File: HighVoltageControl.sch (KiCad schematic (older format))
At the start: 6 parts, among them Q1 DMG2302U, U1 NCS1S1205SC, U7 AZ1117-3.3

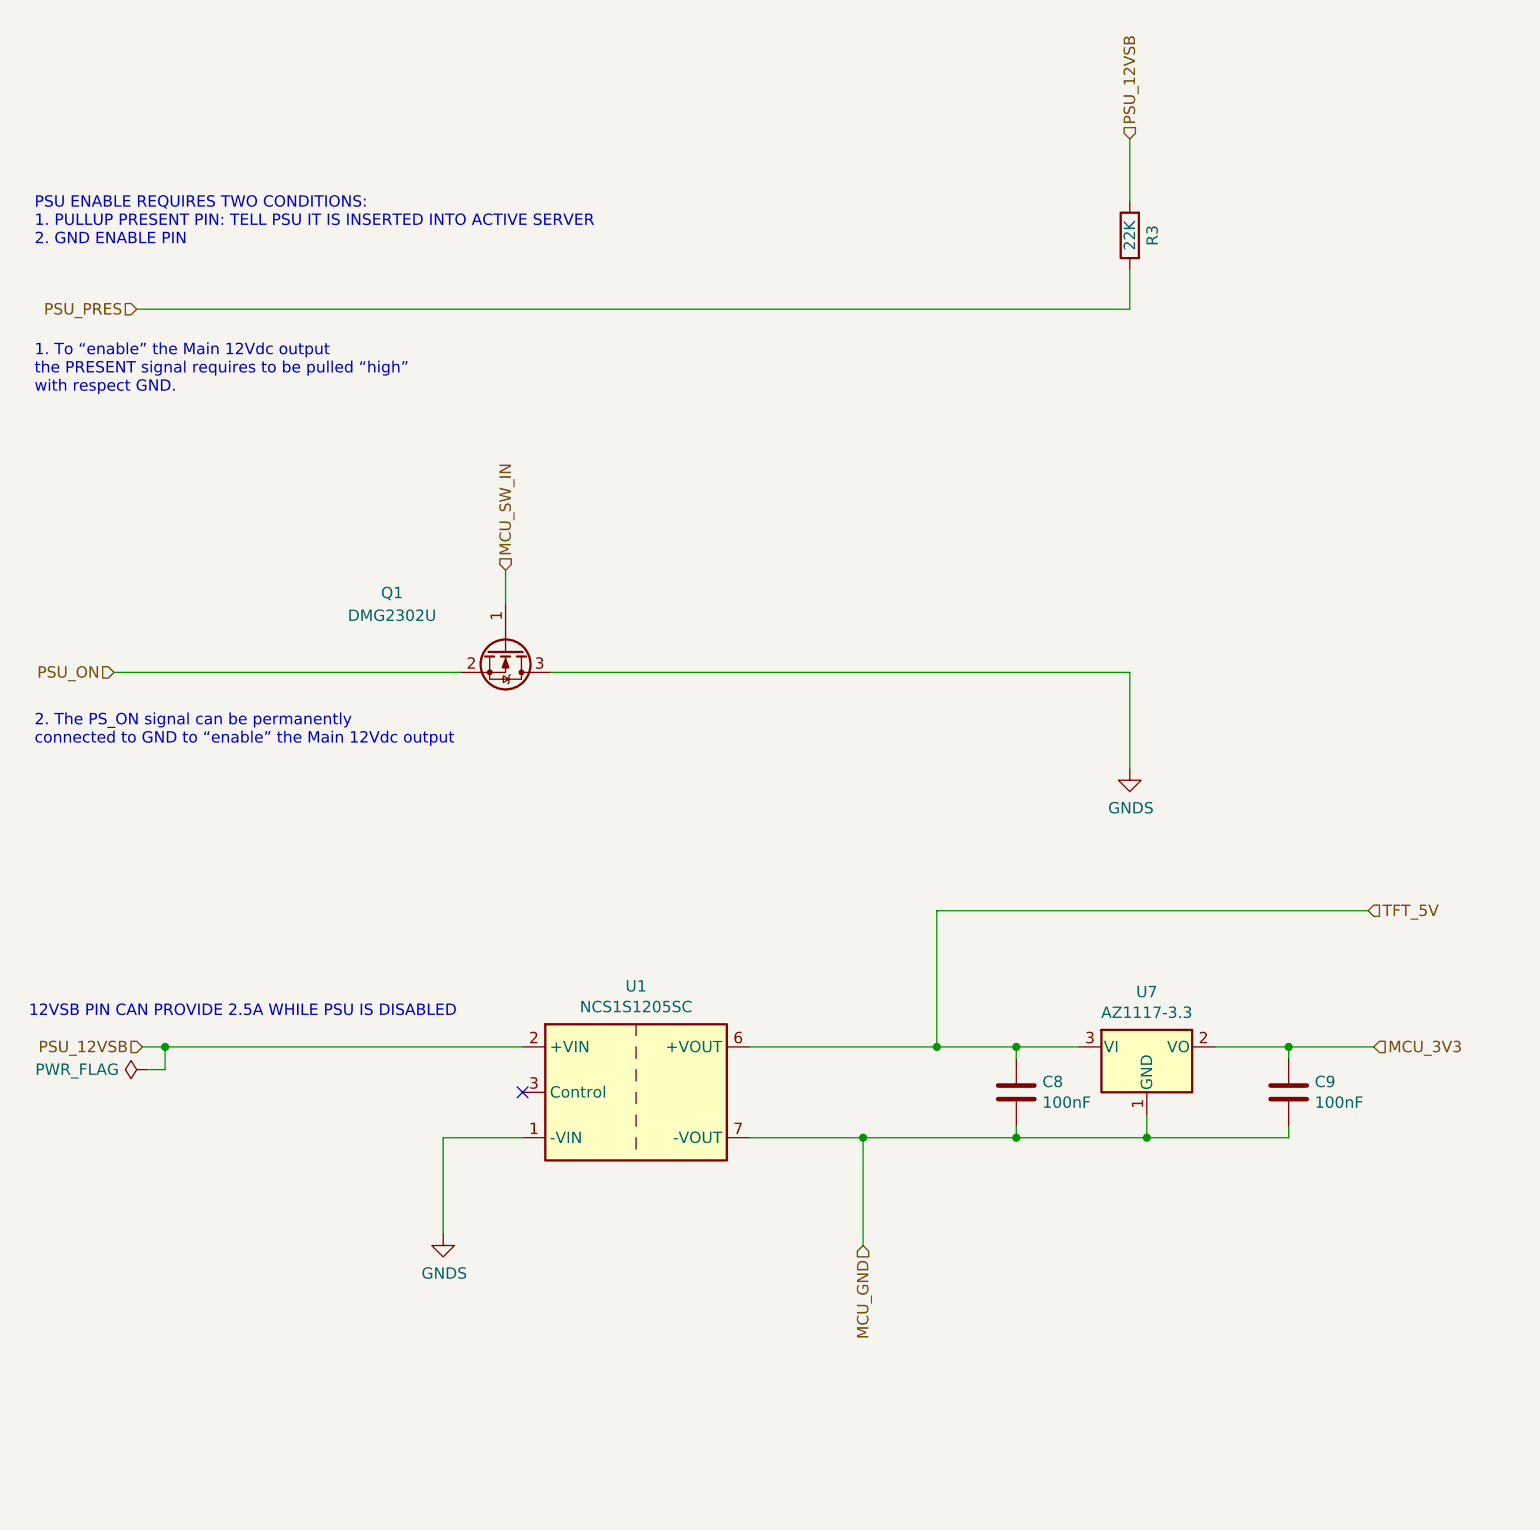
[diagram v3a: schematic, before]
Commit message: updated hw
- added SMBUS address HW 
- Changed Isolated DC Module to TI SimpleSwitcher IC
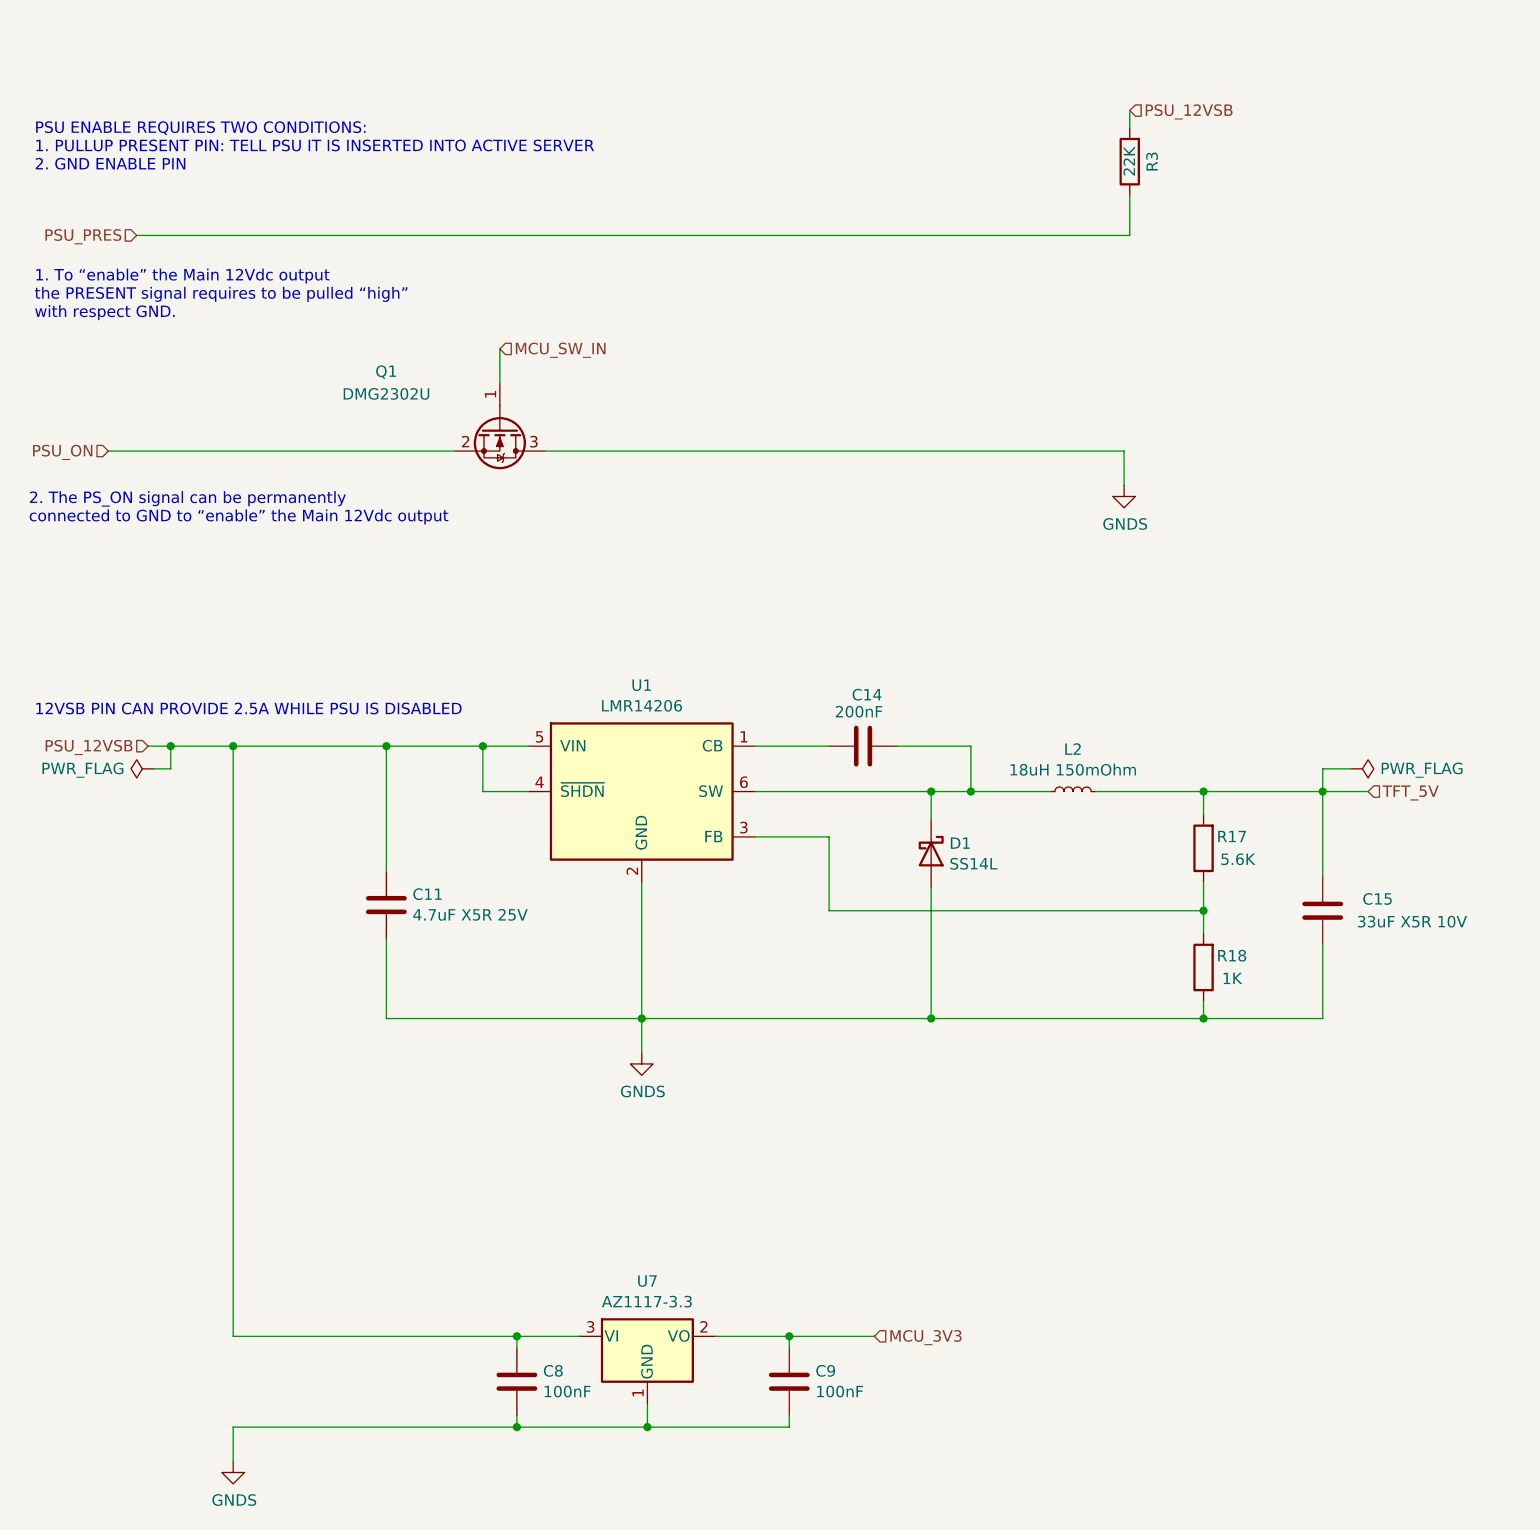
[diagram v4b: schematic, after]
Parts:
- removed U1: NCS1S1205SC, Converter_DCDC:Converter_DCDC_Murata_NCS1SxxxxSC_THT, symbol Converter_DCDC:NCS1S1205SC
- added C11: 4.7uF X5R 25V, Capacitor_SMD:C_0805_2012Metric_Pad1.15x1.40mm_HandSolder, symbol Device:C
- added C14: 200nF, Capacitor_SMD:C_0805_2012Metric_Pad1.15x1.40mm_HandSolder, symbol Device:C
- added C15: 33uF X5R 10V, Capacitor_SMD:C_0805_2012Metric_Pad1.15x1.40mm_HandSolder, symbol Device:C
- added D1: SS14L, Diode_SMD:D_SOD-123F, symbol Device:D_Schottky
- added L2: 18uH 150mOhm, Inductor_SMD:L_Bourns-SRN8040_8x8.15mm, symbol Device:L_Small
- added R17: 5.6K, Resistor_SMD:R_0805_2012Metric_Pad1.15x1.40mm_HandSolder, symbol Device:R
- added R18: 1K, Resistor_SMD:R_0805_2012Metric_Pad1.15x1.40mm_HandSolder, symbol Device:R
- added U1: LMR14206, Package_TO_SOT_SMD:SOT-23-6, symbol Regulator_Switching:LMR14206
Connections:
- net MCU_GND is gone; now on net GNDS: C8.2, C9.2, U7.1 (GND)
- net GNDS: now also C11.2, C15.1, D1.2 (A), R18.1, U1.2 (GND)
- net PSU_12VSB: now also C8.1, U7.3 (VI), C11.1, U1.4 (~SHDN), U1.5 (VIN)
- net TFT_5V: now also C15.2, L2.2, R17.2; no longer C8.1, U7.3 (VI)
- new net: C14.2, U1.1 (CB)
- new net: R17.1, R18.2, U1.3 (FB)
- new net: C14.1, D1.1 (K), L2.1, U1.6 (SW)
- no-connect marks 1 -> 0
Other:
- moved on the sheet: C8, C9, Q1, R3, U7

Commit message: Completed RevA
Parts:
- added TP5, TP6: TestPoint, TestPoint:TestPoint_Pad_1.0x1.0mm, symbol Connector:TestPoint
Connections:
- net GNDS: now also TP6.1
- net TFT_5V: now also TP5.1
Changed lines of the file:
@@
 Wire Wire Line
 	7450 4025 7450 4125
+$Comp
+L Connector:TestPoint TP?
+U 1 1 5F1A3F4D
+P 7450 3800
+AR Path="/5F02F4E9/5F1A3F4D" Ref="TP?"  Part="1"
+AR Path="/5EFF0F4B/5F1A3F4D" Ref="TP?"  Part="1"
+AR Path="/5F02F4C5/5F1A3F4D" Ref="TP5"  Part="1"
+F 0 "TP5" H 7508 3918 50  0000 L CNN
+F 1 "TestPoint" H 7508 3827 50  0000 L CNN
+F 2 "TestPoint:TestPoint_Pad_1.0x1.0mm" H 7650 3800 50  0001 C CNN
+F 3 "~" H 7650 3800 50  0001 C CNN
+	1    7450 3800
+	1    0    0    -1
+$EndComp
+Wire Wire Line
+	7450 3800 7450 4025
+$Comp
+L Connector:TestPoint TP?
+U 1 1 5F1A53E6
+P 7450 5350
+AR Path="/5F02F4E9/5F1A53E6" Ref="TP?"  Part="1"
+AR Path="/5EFF0F4B/5F1A53E6" Ref="TP?"  Part="1"
+AR Path="/5F02F4C5/5F1A53E6" Ref="TP6"  Part="1"
+F 0 "TP6" H 7508 5468 50  0000 L CNN
+F 1 "TestPoint" H 7508 5377 50  0000 L CNN
+F 2 "TestPoint:TestPoint_Pad_1.0x1.0mm" H 7650 5350 50  0001 C CNN
+F 3 "~" H 7650 5350 50  0001 C CNN
+	1    7450 5350
+	-1   0    0    1
+$EndComp
+Wire Wire Line
+	7450 5350 7450 5125
 $EndSCHEMATC

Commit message: backup
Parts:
- U7: value AZ1117-3.3 -> AZ1117CR-3.3
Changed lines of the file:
@@
 P 4475 6525
 F 0 "U7" H 4475 6767 50  0000 C CNN
-F 1 "AZ1117-3.3" H 4475 6676 50  0000 C CNN
+F 1 "AZ1117CR-3.3" H 4475 6676 50  0000 C CNN
 F 2 "Package_TO_SOT_SMD:SOT-89-3_Handsoldering" H 4475 6775 50  0001 C CIN
-F 3 "https://www.diodes.com/assets/Datasheets/AZ1117.pdf" H 4475 6525 50  0001 C CNN
+F 3 "https://www.diodes.com/assets/Datasheets/AZ1117C.pdf" H 4475 6525 50  0001 C CNN
 	1    4475 6525
 	1    0    0    -1
